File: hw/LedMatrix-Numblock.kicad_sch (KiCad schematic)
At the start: 42 parts, among them Q2200 DTA114E, Q2201 DTA114E, Q2202 DTA114E, Q2203 DTA114E, Q2204 DTA114E, Q2205 DTA114E, Q2206 DTC114EE, Q2207 DTC114EE, Q2208 DTC114EE, Q2209 DTC114EE, Q2210 DTC114EE, Q2211 DTC114EE, Q2212 DTC114EE, Q2213 DTC114EE, Q2214 DTC114EE

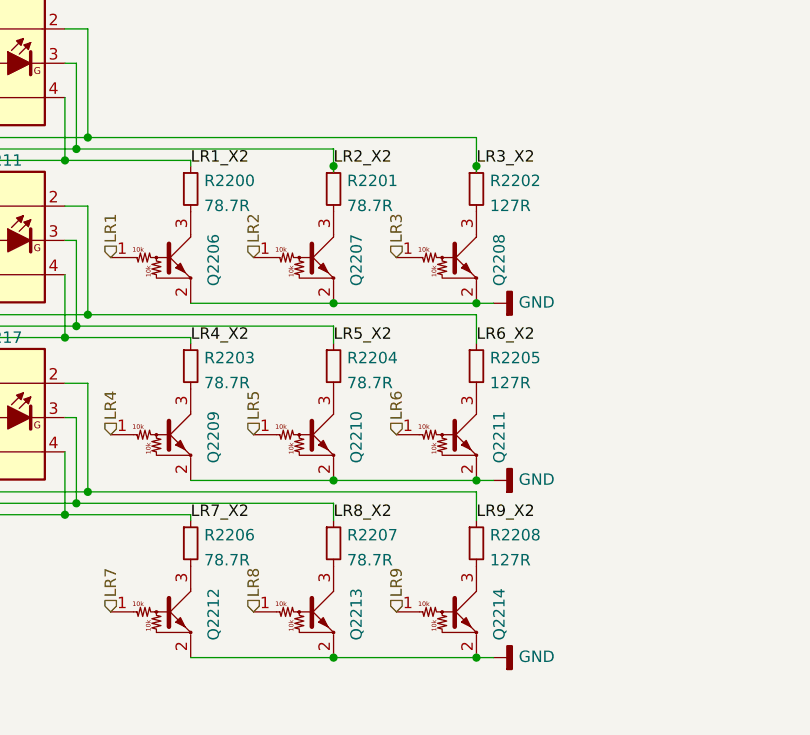
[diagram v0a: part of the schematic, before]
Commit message: Add 300R symbol and use it at green LEDs.
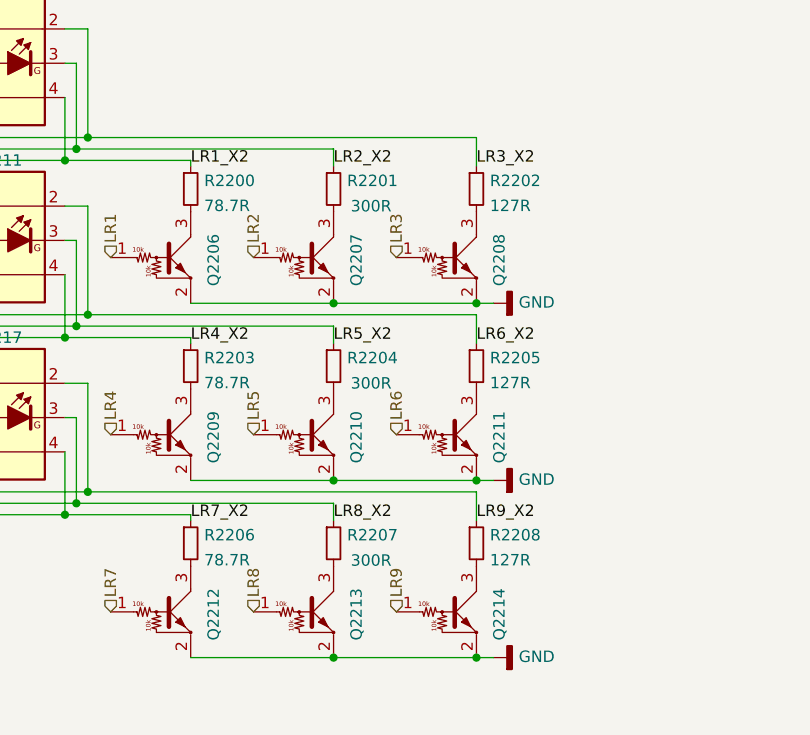
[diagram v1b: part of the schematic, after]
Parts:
- R2201, R2204, R2207: value 78.7R -> 300R; symbol Keyboard:78.7R -> Keyboard:300R; manf# RC0402FR-0778R7L -> ERJ-2RKF3000X; mouser# 603-RC0402FR-0778R7L -> 667-ERJ-2RKF3000X
